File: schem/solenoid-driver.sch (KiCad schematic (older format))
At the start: 25 parts, among them J1 Conn_01x03, J2 SOLENOID, Q1 AO3400, U1 MIC2009A-1, U3 MIC2250-2

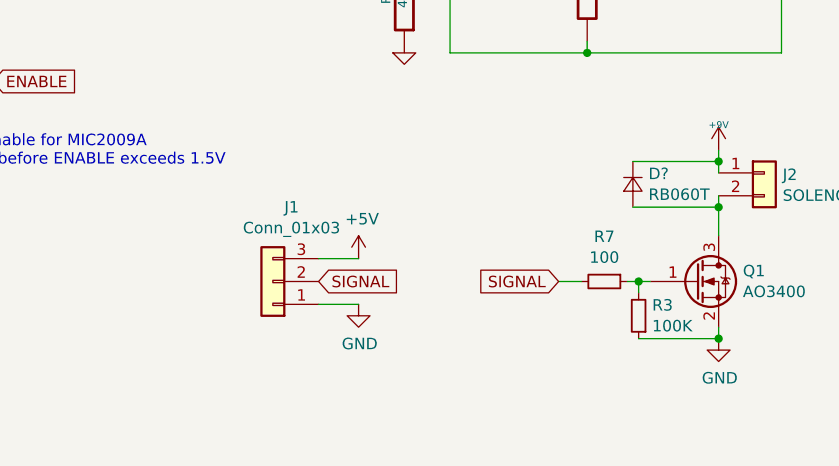
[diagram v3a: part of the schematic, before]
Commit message: Fix pinout and regenerate gerber
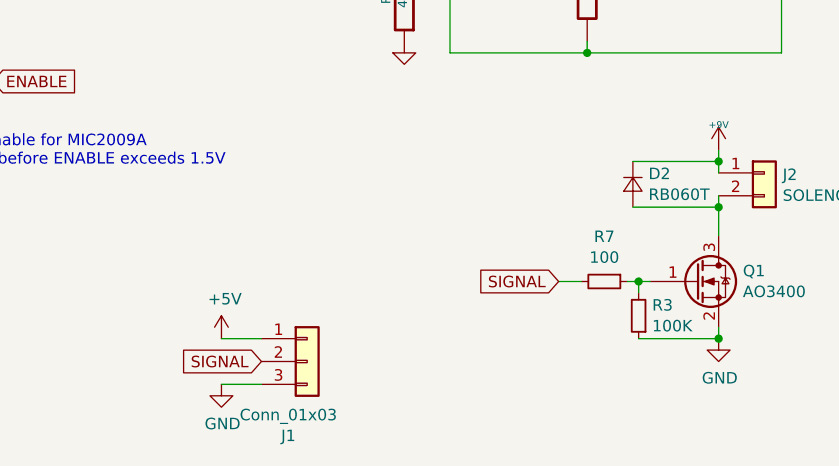
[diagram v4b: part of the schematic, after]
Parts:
- gave numbers to parts that had none: 1
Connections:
- net +5V: now also J1.1 (Pin_1); no longer J1.3 (Pin_3)
- net GND: now also J1.3 (Pin_3); no longer J1.1 (Pin_1)
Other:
- moved on the sheet: J1
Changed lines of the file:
@@
 L Connector_Generic:Conn_01x03 J1
 U 1 1 5E7C9766
-P 4075 4350
-F 0 "J1" H 3993 4025 50  0000 C CNN
-F 1 "Conn_01x03" H 3993 4116 50  0000 C CNN
-F 2 "random-keyboard-parts:JST-SR-3" H 4075 4350 50  0001 C CNN
-F 3 "~" H 4075 4350 50  0001 C CNN
-	1    4075 4350
-	-1   0    0    1
-$EndComp
-Text GLabel 4275 4350 2    50   Input ~ 0
+P 4225 4700
+F 0 "J1" H 4143 4375 50  0000 C CNN
+F 1 "Conn_01x03" H 4143 4466 50  0000 C CNN
+F 2 "random-keyboard-parts:JST-SR-3" H 4225 4700 50  0001 C CNN
+F 3 "~" H 4225 4700 50  0001 C CNN
+	1    4225 4700
+	1    0    0    -1
+$EndComp
+Text GLabel 4025 4700 0    50   Input ~ 0
 SIGNAL
 $Comp
 L power:+5V #PWR0101
 U 1 1 5E7CB7F0
-P 4450 4250
-F 0 "#PWR0101" H 4450 4100 50  0001 C CNN
-F 1 "+5V" H 4465 4423 50  0000 C CNN
-F 2 "" H 4450 4250 50  0001 C CNN
-F 3 "" H 4450 4250 50  0001 C CNN
-	1    4450 4250
-	1    0    0    -1
-$EndComp
-Wire Wire Line
-	4450 4250 4275 4250
+P 3850 4600
+F 0 "#PWR0101" H 3850 4450 50  0001 C CNN
+F 1 "+5V" H 3865 4773 50  0000 C CNN
+F 2 "" H 3850 4600 50  0001 C CNN
+F 3 "" H 3850 4600 50  0001 C CNN
+	1    3850 4600
+	1    0    0    -1
+$EndComp
+Wire Wire Line
+	3850 4800 4025 4800
 $Comp
 L power:GND #PWR0102
 U 1 1 5E7CDEDA
-P 4450 4450
-F 0 "#PWR0102" H 4450 4200 50  0001 C CNN
-F 1 "GND" H 4455 4277 50  0000 C CNN
-F 2 "" H 4450 4450 50  0001 C CNN
-F 3 "" H 4450 4450 50  0001 C CNN
-	1    4450 4450
-	1    0    0    -1
-$EndComp
-Wire Wire Line
-	4450 4450 4275 4450
+P 3850 4800
+F 0 "#PWR0102" H 3850 4550 50  0001 C CNN
+F 1 "GND" H 3855 4627 50  0000 C CNN
+F 2 "" H 3850 4800 50  0001 C CNN
+F 3 "" H 3850 4800 50  0001 C CNN
+	1    3850 4800
+	1    0    0    -1
+$EndComp
+Wire Wire Line
+	3850 4600 4025 4600
 Text GLabel 5325 4350 0    50   Input ~ 0
 SIGNAL
@@
 	5325 4350 5425 4350
 $Comp
-L Device:D_Small D?
+L Device:D_Small D2
 U 1 1 5E8BE98D
 P 5650 3925
-F 0 "D?" V 5604 3993 50  0000 L CNN
+F 0 "D2" V 5604 3993 50  0000 L CNN
 F 1 "RB060T" V 5695 3993 50  0000 L CNN
 F 2 "Diode_SMD:D_SOD-123" V 5650 3925 50  0001 C CNN
